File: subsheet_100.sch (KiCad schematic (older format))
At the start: 16 parts, among them P100 1K2 ×8, P101 4K7 ×8, P102 4K7 ×8, P103 4K7 ×8, P104 10K ×8, P105 10K ×8, U100 MC68000_PLCC_68_PHY

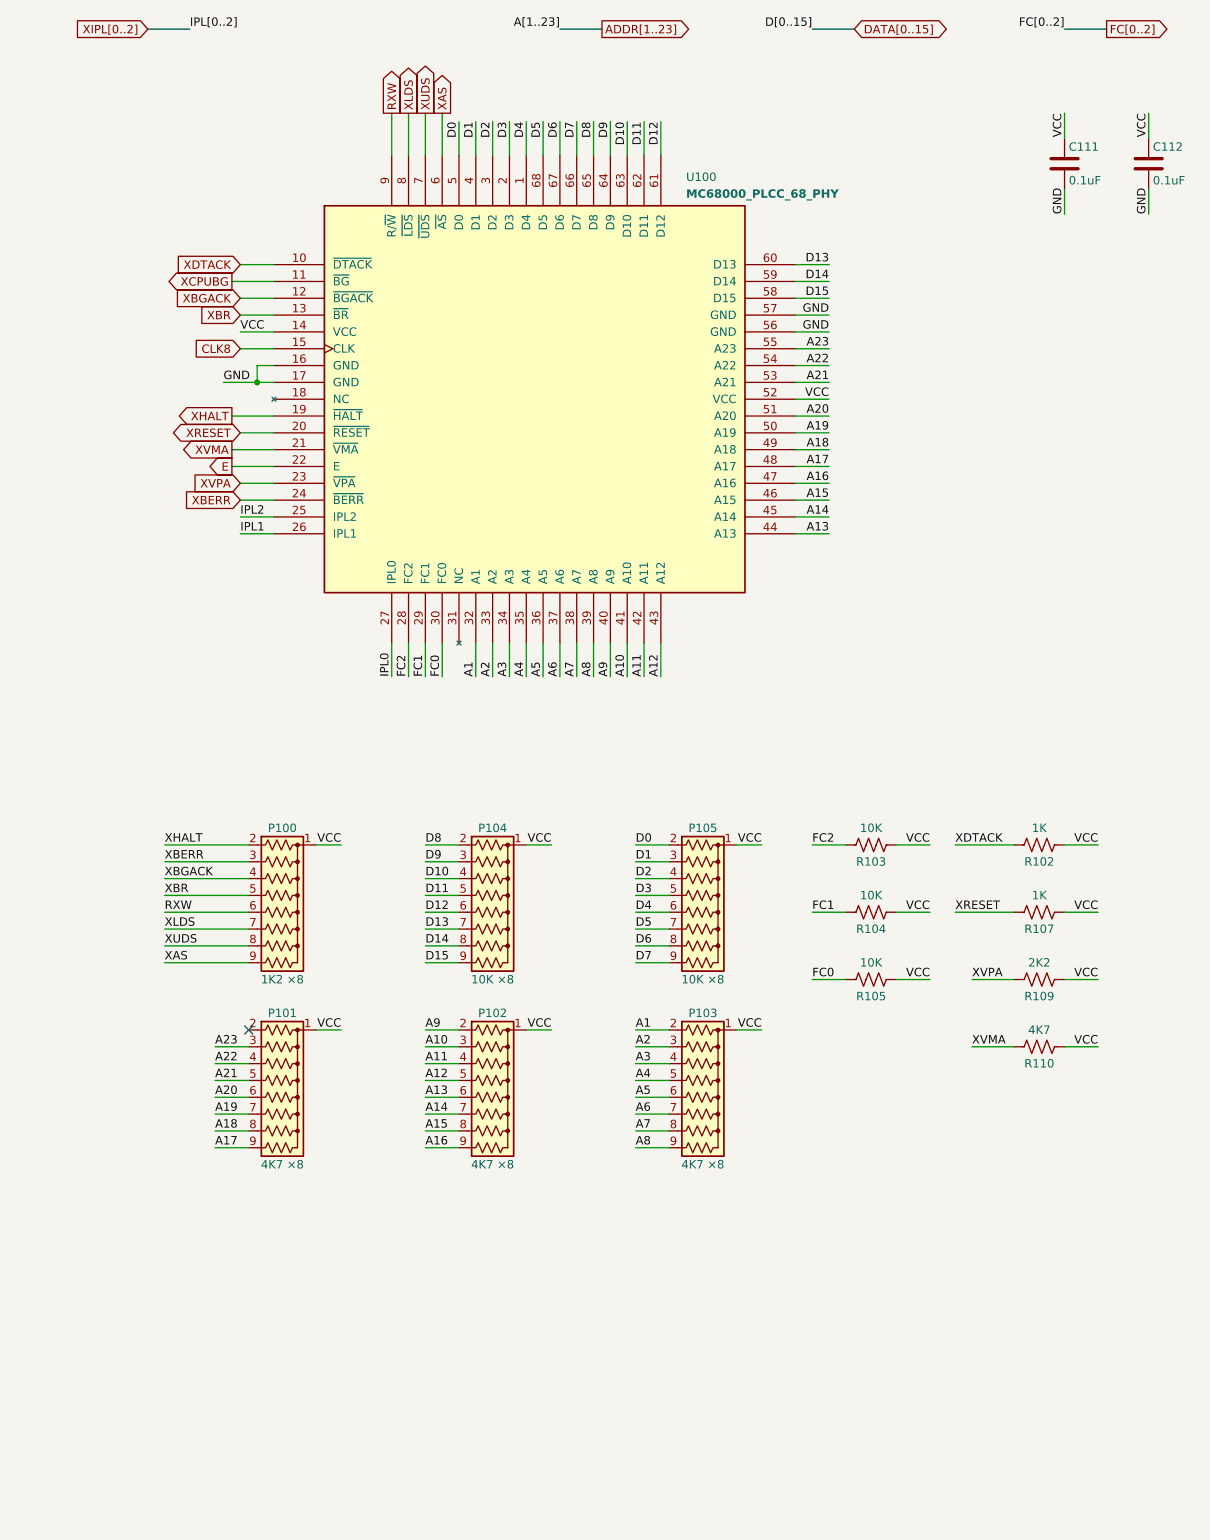
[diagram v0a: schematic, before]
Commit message: Added DIP-64 CPU port extension
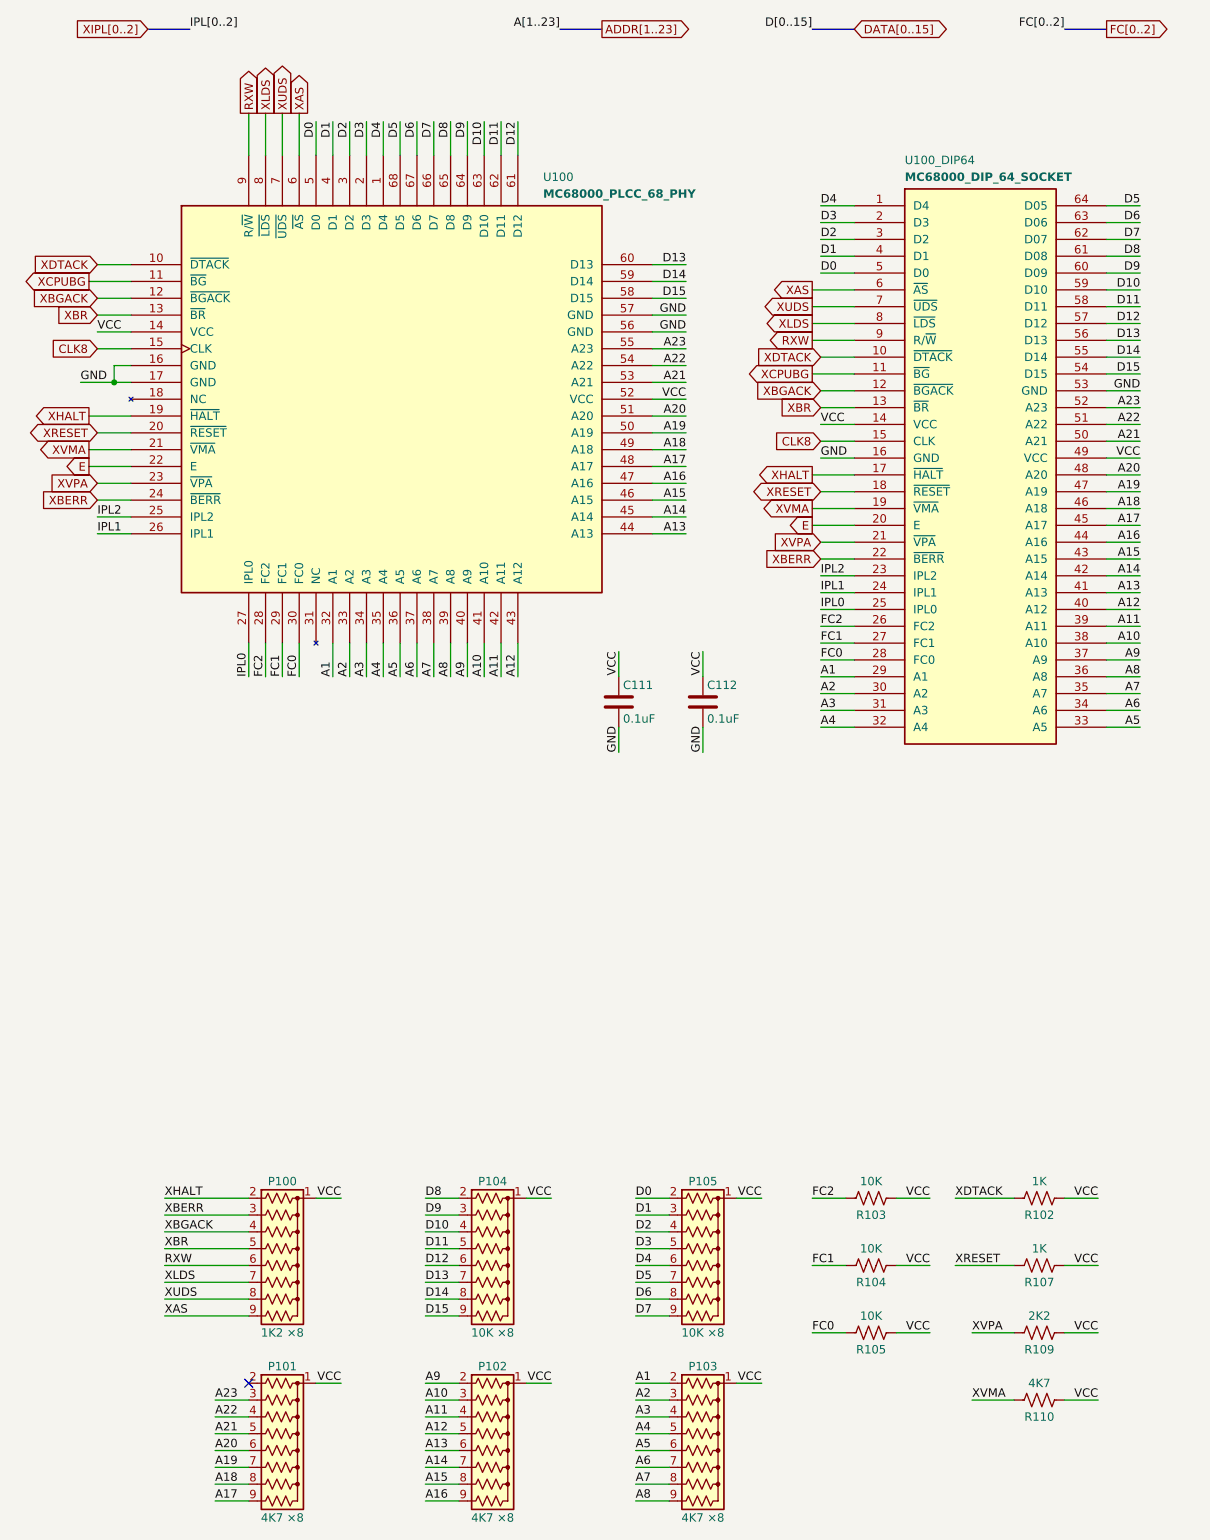
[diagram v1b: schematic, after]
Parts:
- added U100_DIP64: MC68000_DIP_64_SOCKET, Package_DIP:DIP-64_W15.24mm_LongPads, symbol mc_68000_dip64:MC68000_DIP_64_SOCKET
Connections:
- net A1: now also U100_DIP64.29 (A1)
- net A10: now also U100_DIP64.38 (A10)
- net A11: now also U100_DIP64.39 (A11)
- net A12: now also U100_DIP64.40 (A12)
- net A13: now also U100_DIP64.41 (A13)
- net A14: now also U100_DIP64.42 (A14)
- net A15: now also U100_DIP64.43 (A15)
- net A16: now also U100_DIP64.44 (A16)
- net A17: now also U100_DIP64.45 (A17)
- net A18: now also U100_DIP64.46 (A18)
- net A19: now also U100_DIP64.47 (A19)
- net A2: now also U100_DIP64.30 (A2)
- net A20: now also U100_DIP64.48 (A20)
- net A21: now also U100_DIP64.50 (A21)
- net A22: now also U100_DIP64.51 (A22)
- net A23: now also U100_DIP64.52 (A23)
- net A3: now also U100_DIP64.31 (A3)
- net A4: now also U100_DIP64.32 (A4)
- net A5: now also U100_DIP64.33 (A5)
- net A6: now also U100_DIP64.34 (A6)
- net A7: now also U100_DIP64.35 (A7)
- net A8: now also U100_DIP64.36 (A8)
- net A9: now also U100_DIP64.37 (A9)
- net CLK8: now also U100_DIP64.15 (CLK)
- net D0: now also U100_DIP64.5 (D0)
- net D1: now also U100_DIP64.4 (D1)
- net D10: now also U100_DIP64.59 (D10)
- net D11: now also U100_DIP64.58 (D11)
- net D12: now also U100_DIP64.57 (D12)
- net D13: now also U100_DIP64.56 (D13)
- net D14: now also U100_DIP64.55 (D14)
- net D15: now also U100_DIP64.54 (D15)
- net D2: now also U100_DIP64.3 (D2)
- net D3: now also U100_DIP64.2 (D3)
- net D4: now also U100_DIP64.1 (D4)
- net D5: now also U100_DIP64.64 (D05)
- net D6: now also U100_DIP64.63 (D06)
- net D7: now also U100_DIP64.62 (D07)
- net D8: now also U100_DIP64.61 (D08)
- net D9: now also U100_DIP64.60 (D09)
- net E: now also U100_DIP64.20 (E)
- net FC0: now also U100_DIP64.28 (FC0)
- net FC1: now also U100_DIP64.27 (FC1)
- net FC2: now also U100_DIP64.26 (FC2)
- net GND: now also U100_DIP64.16 (GND), U100_DIP64.53 (GND)
- net IPL0: now also U100_DIP64.25 (IPL0)
- net IPL1: now also U100_DIP64.24 (IPL1)
- net IPL2: now also U100_DIP64.23 (IPL2)
- net RXW: now also U100_DIP64.9 (R/~W~)
- net VCC: now also U100_DIP64.14 (VCC), U100_DIP64.49 (VCC)
- net XAS: now also U100_DIP64.6 (~AS~)
- net XBERR: now also U100_DIP64.22 (~BERR~)
- net XBGACK: now also U100_DIP64.12 (~BGACK~)
- net XBR: now also U100_DIP64.13 (~BR~)
- net XCPUBG: now also U100_DIP64.11 (~BG~)
- net XDTACK: now also U100_DIP64.10 (~DTACK~)
- net XHALT: now also U100_DIP64.17 (~HALT~)
- net XLDS: now also U100_DIP64.8 (~LDS~)
- net XRESET: now also U100_DIP64.18 (~RESET~)
- net XUDS: now also U100_DIP64.7 (~UDS~)
- net XVMA: now also U100_DIP64.19 (~VMA~)
- net XVPA: now also U100_DIP64.21 (~VPA~)
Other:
- moved on the sheet: C111, C112, P100, P101, P102, P103, P104, P105, R102, R103, R104, R105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

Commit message: removed the external blitter
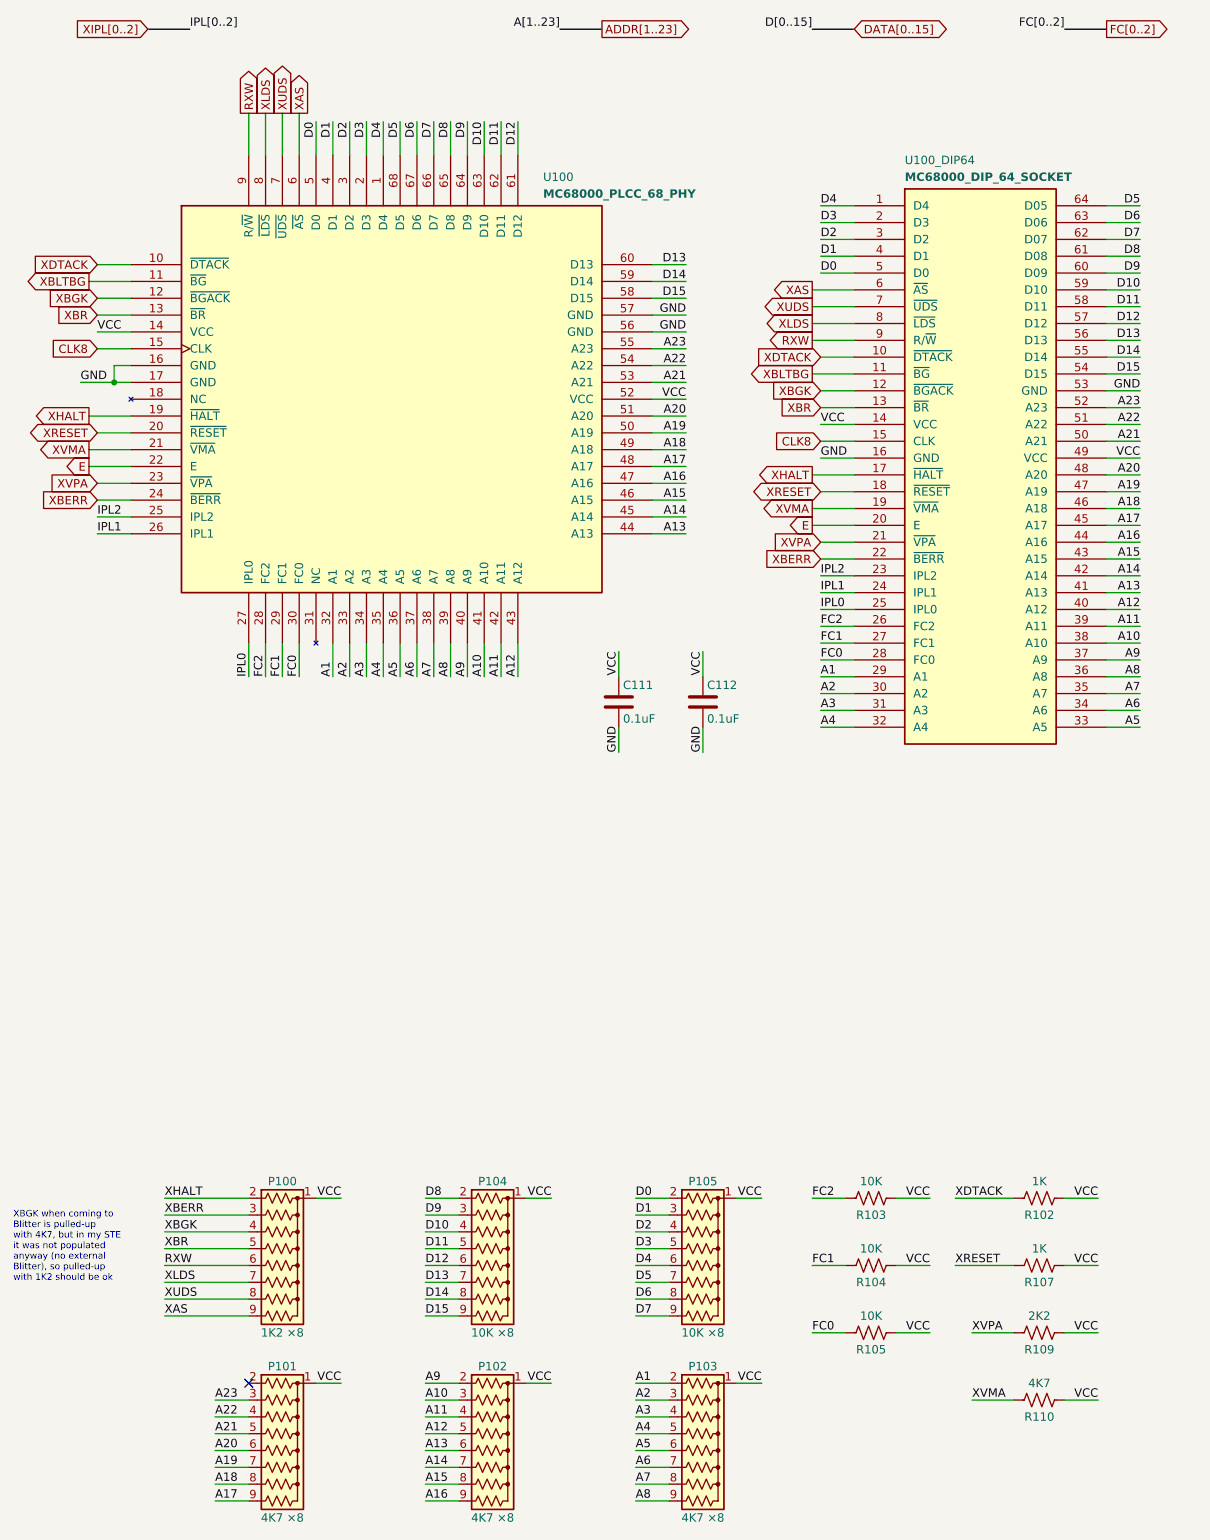
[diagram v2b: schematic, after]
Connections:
- net XBGACK renamed XBGK
- net XCPUBG renamed XBLTBG
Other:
- note added: "XBGK when coming to \nBlitter is pulled-up\nwith 4K7, but in my STE\nit was not populated \nanyway (no external\nBlitter), so pulled-up \nwith 1K2 should be ok"
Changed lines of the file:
@@
 XLDS
 Text GLabel 950  2500 0    50   Output ~ 0
-XCPUBG
+XBLTBG
 Wire Bus Line
 	1300 1000 1550 1000
@@
 XBERR
 Text Label 1400 8150 0    50   ~ 0
-XBGACK
+XBGK
 Text Label 1400 8250 0    50   ~ 0
 XBR
@@
 XBR
 Text GLabel 1000 2600 0    50   Input ~ 0
-XBGACK
+XBGK
 Text GLabel 1000 2400 0    50   Input ~ 0
 XDTACK
@@
 VCC
 Text GLabel 5250 3050 0    50   Output ~ 0
-XCPUBG
+XBLTBG
 Text GLabel 5300 3450 0    50   Input ~ 0
 CLK8
@@
 XBR
 Text GLabel 5300 3150 0    50   Input ~ 0
-XBGACK
+XBGK
 Text GLabel 5300 2950 0    50   Input ~ 0
 XDTACK
@@
 	1    0    0    -1
 $EndComp
+Text Notes 500  8450 0    39   ~ 0
+XBGK when coming to \nBlitter is pulled-up\nwith 4K7, but in my STE\nit was not populated \nanyway (no external\nBlitter), so pulled-up \nwith 1K2 should be ok
 $EndSCHEMATC

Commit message: Resolves #1 : Use 4-resistor packs wherever it is possible
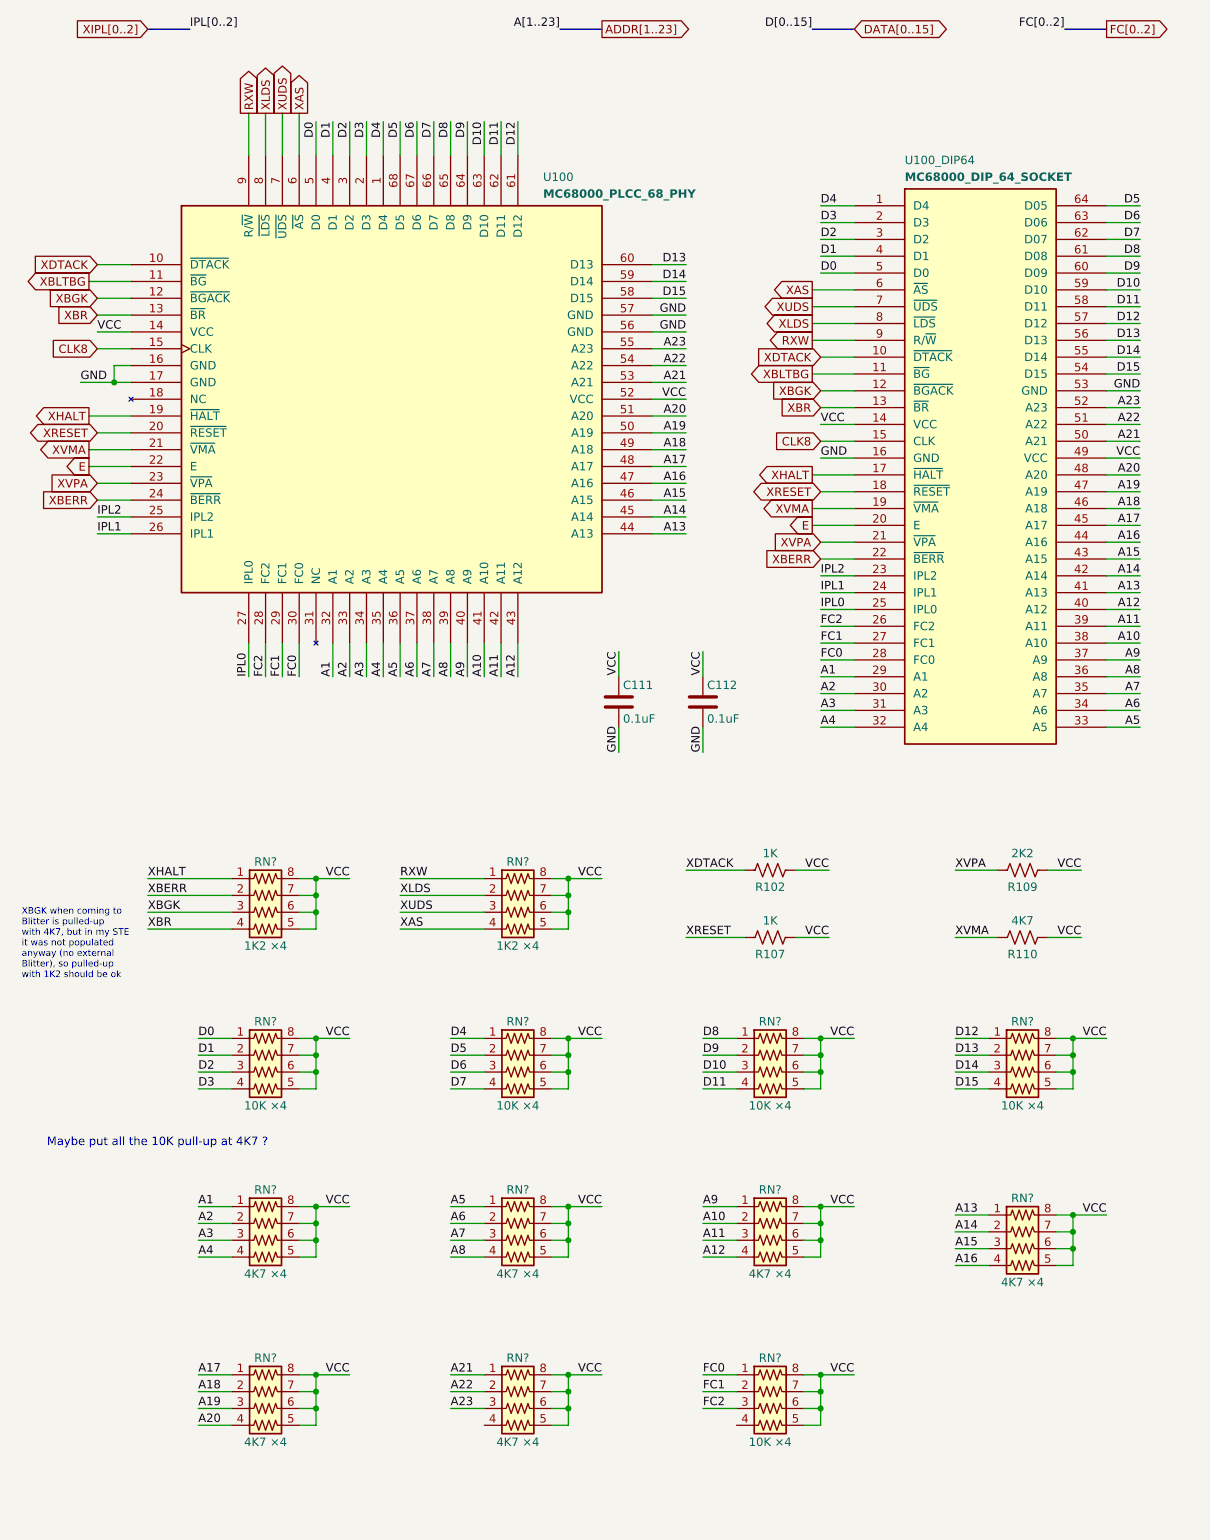
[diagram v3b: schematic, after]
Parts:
- removed P100: 1K2 ×8, Resistor_THT:R_Array_SIP9, symbol Device:R_Network08_US
- removed P101, P102, P103: 4K7 ×8, Resistor_THT:R_Array_SIP9, symbol Device:R_Network08_US
- removed P104, P105: 10K ×8, Resistor_THT:R_Array_SIP9, symbol Device:R_Network08_US
- removed R103, R104, R105: 10K, commons_passives_THT:Passive_THT_resistor_W2.54mm_L12.70mm, symbol Device:R_US
- added RN? (x2): 1K2 ×4, symbol custom_passives:R_Pack04_US
- added RN? (x5): 10K ×4, symbol custom_passives:R_Pack04_US
- added RN? (x6): 4K7 ×4, symbol custom_passives:R_Pack04_US
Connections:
- net A1: now also RN?.1 (R1.1)
- net A10: now also RN?.2 (R2.1)
- net A11: now also RN?.3 (R3.1)
- net A12: now also RN?.4 (R4.1)
- net A13: now also RN?.1 (R1.1)
- net A14: now also RN?.2 (R2.1)
- net A15: now also RN?.3 (R3.1)
- net A16: now also RN?.4 (R4.1)
- net A17: now also RN?.1 (R1.1)
- net A18: now also RN?.2 (R2.1)
- net A19: now also RN?.3 (R3.1)
- net A2: now also RN?.2 (R2.1)
- net A20: now also RN?.4 (R4.1)
- net A21: now also RN?.1 (R1.1)
- net A22: now also RN?.2 (R2.1)
- net A23: now also RN?.3 (R3.1)
- net A3: now also RN?.3 (R3.1)
- net A4: now also RN?.4 (R4.1)
- net A5: now also RN?.1 (R1.1)
- net A6: now also RN?.2 (R2.1)
- net A7: now also RN?.3 (R3.1)
- net A8: now also RN?.4 (R4.1)
- net A9: now also RN?.1 (R1.1)
- net D0: now also RN?.1 (R1.1)
- net D1: now also RN?.2 (R2.1)
- net D10: now also RN?.3 (R3.1)
- net D11: now also RN?.4 (R4.1)
- net D12: now also RN?.1 (R1.1)
- net D13: now also RN?.2 (R2.1)
- net D14: now also RN?.3 (R3.1)
- net D15: now also RN?.4 (R4.1)
- net D2: now also RN?.3 (R3.1)
- net D3: now also RN?.4 (R4.1)
- net D4: now also RN?.1 (R1.1)
- net D5: now also RN?.2 (R2.1)
- net D6: now also RN?.3 (R3.1)
- net D7: now also RN?.4 (R4.1)
- net D8: now also RN?.1 (R1.1)
- net D9: now also RN?.2 (R2.1)
- net FC0: now also RN?.1 (R1.1)
- net FC1: now also RN?.2 (R2.1)
- net FC2: now also RN?.3 (R3.1)
- net RXW: now also RN?.1 (R1.1)
- net VCC: now also RN?.5 (R4.2), RN?.5 (R4.2), RN?.5 (R4.2), RN?.5 (R4.2), RN?.5 (R4.2), RN?.5 (R4.2), RN?.5 (R4.2), RN?.5 (R4.2), RN?.5 (R4.2), RN?.5 (R4.2), RN?.5 (R4.2), RN?.5 (R4.2), RN?.5 (R4.2), RN?.6 (R3.2), RN?.6 (R3.2), RN?.6 (R3.2), RN?.6 (R3.2), RN?.6 (R3.2), RN?.6 (R3.2), RN?.6 (R3.2), RN?.6 (R3.2), RN?.6 (R3.2), RN?.6 (R3.2), RN?.6 (R3.2), RN?.6 (R3.2), RN?.6 (R3.2), RN?.7 (R2.2), RN?.7 (R2.2), RN?.7 (R2.2), RN?.7 (R2.2), RN?.7 (R2.2), RN?.7 (R2.2), RN?.7 (R2.2), RN?.7 (R2.2), RN?.7 (R2.2), RN?.7 (R2.2), RN?.7 (R2.2), RN?.7 (R2.2), RN?.7 (R2.2), RN?.8 (R1.2), RN?.8 (R1.2), RN?.8 (R1.2), RN?.8 (R1.2), RN?.8 (R1.2), RN?.8 (R1.2), RN?.8 (R1.2), RN?.8 (R1.2), RN?.8 (R1.2), RN?.8 (R1.2), RN?.8 (R1.2), RN?.8 (R1.2), RN?.8 (R1.2)
- net XAS: now also RN?.4 (R4.1)
- net XBERR: now also RN?.2 (R2.1)
- net XBGK: now also RN?.3 (R3.1)
- net XBR: now also RN?.4 (R4.1)
- net XHALT: now also RN?.1 (R1.1)
- net XLDS: now also RN?.2 (R2.1)
- net XUDS: now also RN?.3 (R3.1)
- no-connect marks 1 -> 0
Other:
- note added: "Maybe put all the 10K pull-up at 4K7 ?"
- moved on the sheet: R102, R107, R109, R110
